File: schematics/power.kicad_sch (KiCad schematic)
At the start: 30 parts, among them J1 9VRMS_60HZ, SW1 SW_SPDT, SW2 SW_Push, SW3 SW_Push, SW4 SW_Push, U1 74HC14, U2 LM2576T-ADJ

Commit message: preliminary PCB design
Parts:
- added H1, H2, H3, H4: MountingHole, MountingHole:MountingHole_3.2mm_M3, symbol Mechanical:MountingHole
- C3, C4, C6, C7: footprint Capacitor_THT:C_Disc_D5.1mm_W3.2mm_P5.00mm -> bvclock:THT_Cap
- D2, D3, D4, D6, D7: footprint Diode_THT:D_DO-35_SOD27_P7.62mm_Horizontal -> bvclock:THT_D_Vertical
- D5: footprint Diode_THT:D_DO-201_P15.24mm_Horizontal -> Diode_THT:D_DO-201AD_P3.81mm_Vertical_CathodeUp
- R1, R2, R3, R4, R5, R6: footprint Resistor_THT:R_Axial_DIN0207_L6.3mm_D2.5mm_P7.62mm_Horizontal -> bvclock:THT_R_Vertical
- U2: footprint Package_TO_SOT_THT:TO-220-5_Vertical -> Package_TO_SOT_THT:TO-220-5_P3.4x3.7mm_StaggerEven_Lead3.8mm_Vertical
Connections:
- net +3V3: now also C5.1, L1.2, R3.1
- net +9VA: now also R1.2; no longer R1.1
- net GND: now also R4.1; no longer R4.2
- net at D2.2 (A), D3.1 (K), U1.1: now also R1.1; no longer R1.2
- net at R3.2, U2.4 (FB): now also R4.2; no longer R4.1
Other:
- moved on the sheet: R1

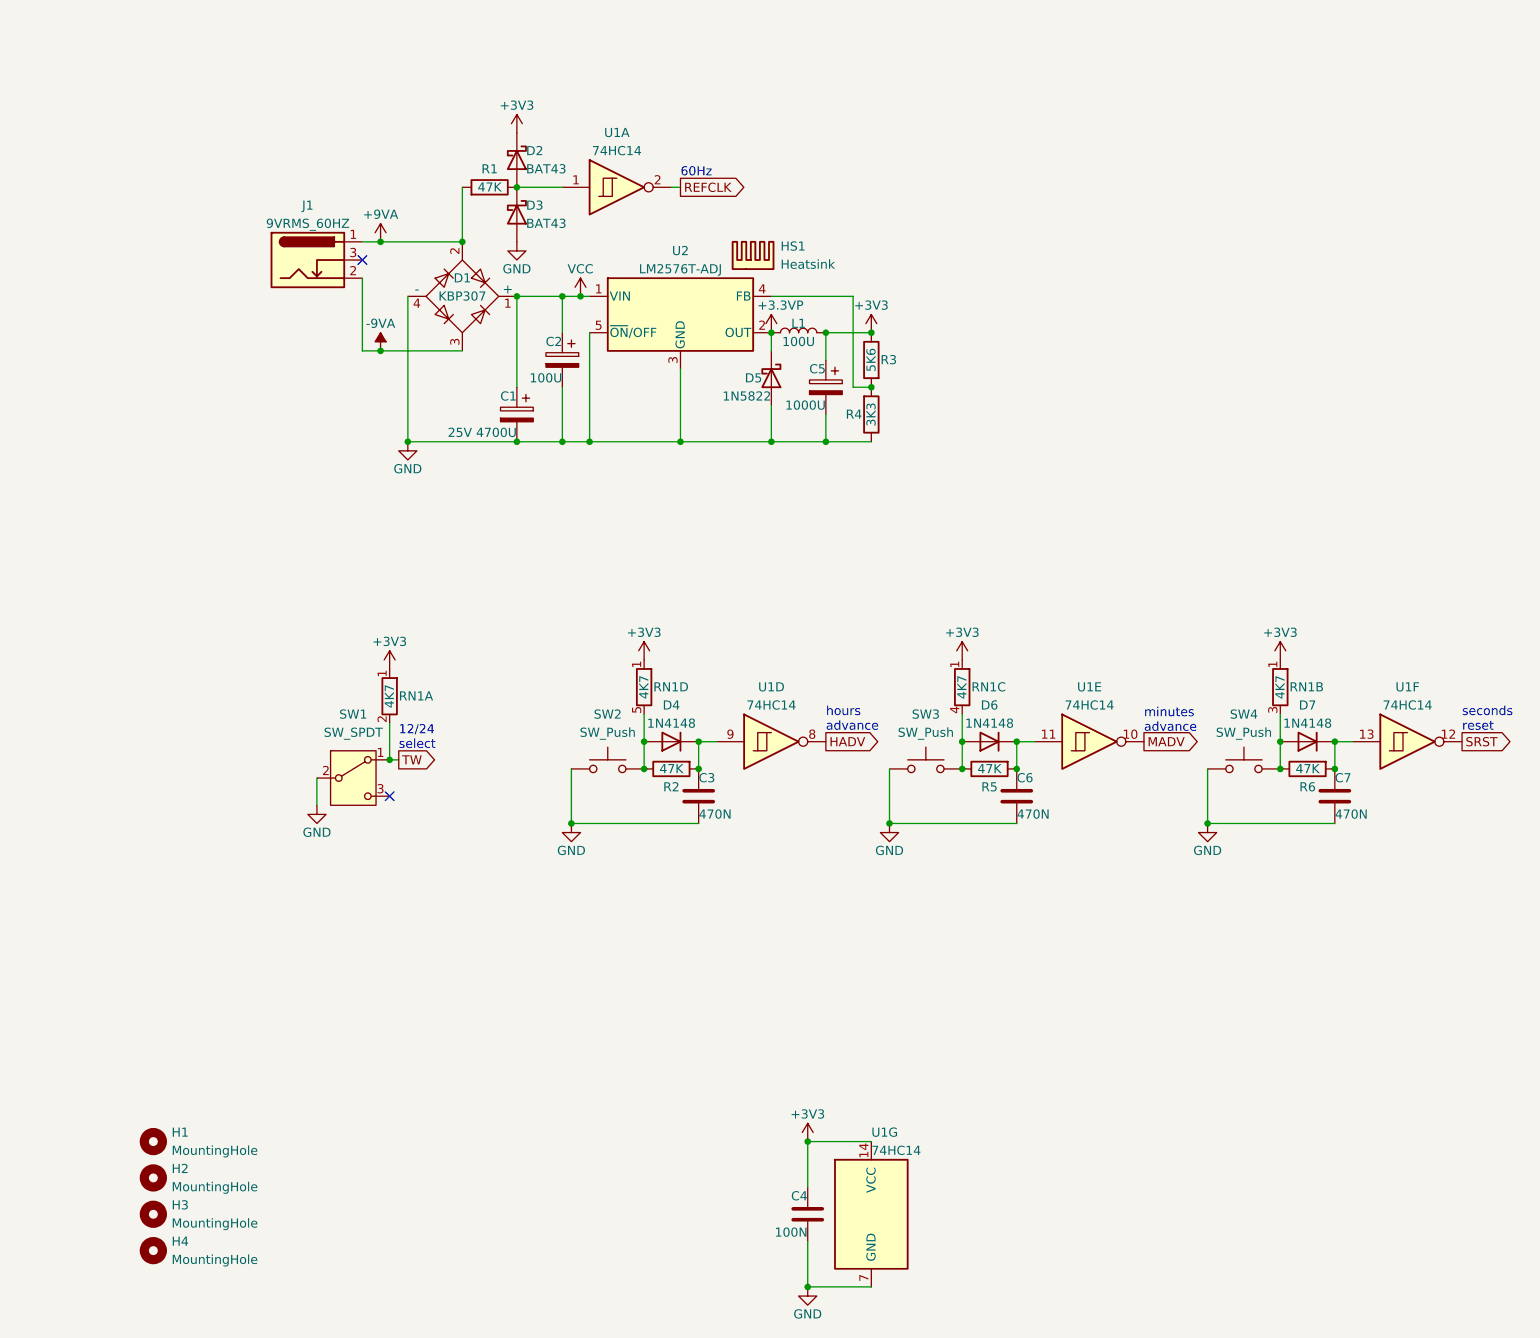
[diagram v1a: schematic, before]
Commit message: passes DRC
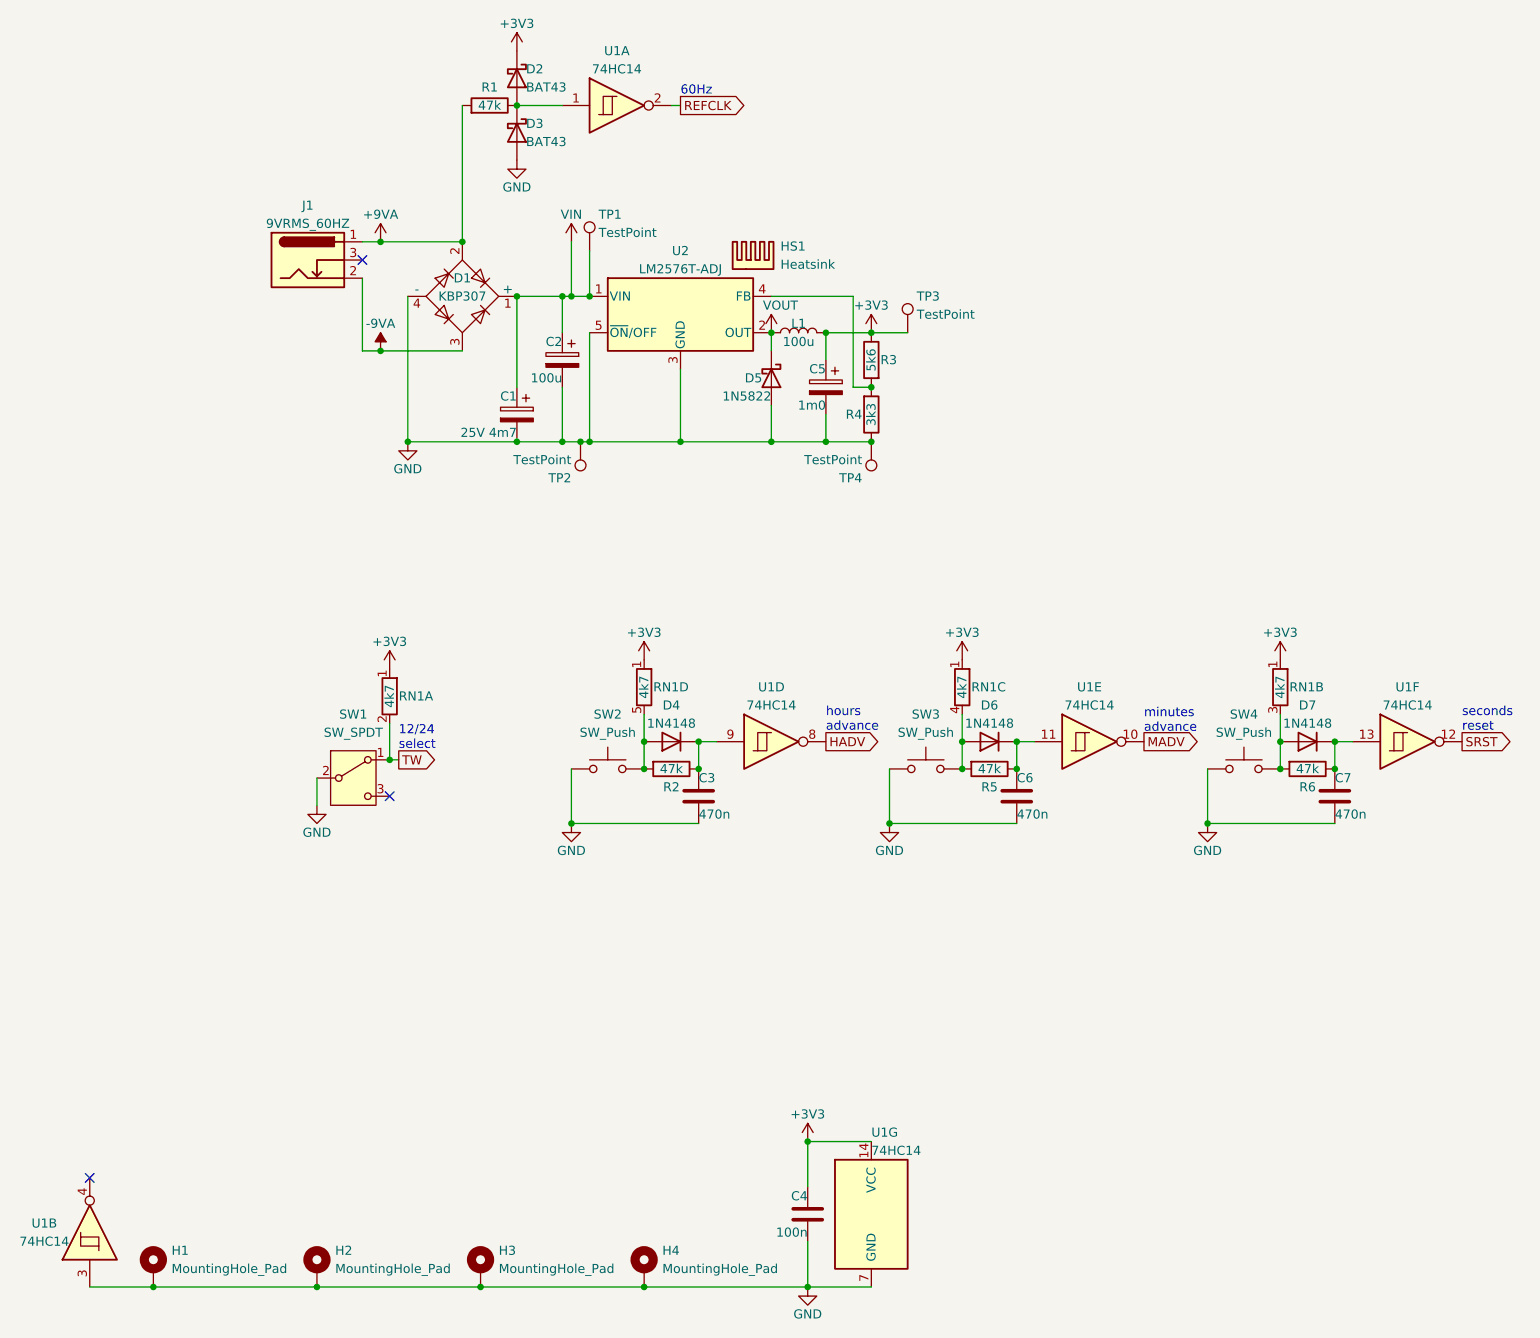
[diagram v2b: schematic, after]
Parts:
- removed H1, H2, H3, H4: MountingHole, MountingHole:MountingHole_3.2mm_M3, symbol Mechanical:MountingHole
- added H1, H2, H3, H4: MountingHole_Pad, MountingHole:MountingHole_2.2mm_M2_ISO7380_Pad_TopBottom, symbol Mechanical:MountingHole_Pad
- added TP1, TP3: TestPoint, bvclock:TestPoint_THTPad_2.5x2.5mm_Drill1.2mm, symbol Connector:TestPoint
- added TP2, TP4: TestPoint, bvclock:TestPoint_THTPad_D1.0mm_Drill0.5mm, symbol Connector:TestPoint
- added unit 2 of U1
- C1: value 25V 4700U -> 25V 4m7
- C2, L1: value 100U -> 100u
- C3, C6, C7: value 470N -> 470n
- C4: value 100N -> 100n
- C5: value 1000U -> 1m0
- D5: footprint Diode_THT:D_DO-201AD_P3.81mm_Vertical_CathodeUp -> Diode_THT:D_DO-201AD_P15.24mm_Horizontal
- J1: footprint Connector_BarrelJack:BarrelJack_Horizontal -> bvclock:BarrelJack_Horizontal
- R1, R2, R5, R6: value 47K -> 47k
- R3: value 5K6 -> 5k6
- R4: value 3K3 -> 3k3
- RN1: value 4K7 -> 4k7
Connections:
- net +3V3: now also TP3.1
- net GND: now also H1.1, H2.1, H3.1, H4.1, TP2.1, TP4.1, U1.3
- net at C3.1, D4.1 (K), U1.9: now also R2.1; no longer R2.2
- net at D6.2 (A), RN1.4 (R3.2), SW3.2: now also R5.2; no longer R5.1
- net at D4.2 (A), RN1.5 (R4.2), SW2.2: now also R2.2; no longer R2.1
- net at D7.2 (A), RN1.3 (R2.2), SW4.2: now also R6.2; no longer R6.1
- net at C6.1, D6.1 (K), U1.11: now also R5.1; no longer R5.2
- net at C7.1, D7.1 (K), U1.13: now also R6.1; no longer R6.2
- net +3.3VP renamed VOUT
- net VCC renamed VIN
- net VIN: now also TP1.1
- no-connect marks 2 -> 3
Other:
- moved on the sheet: D2, D3, R1, R2, R5, R6, U1A

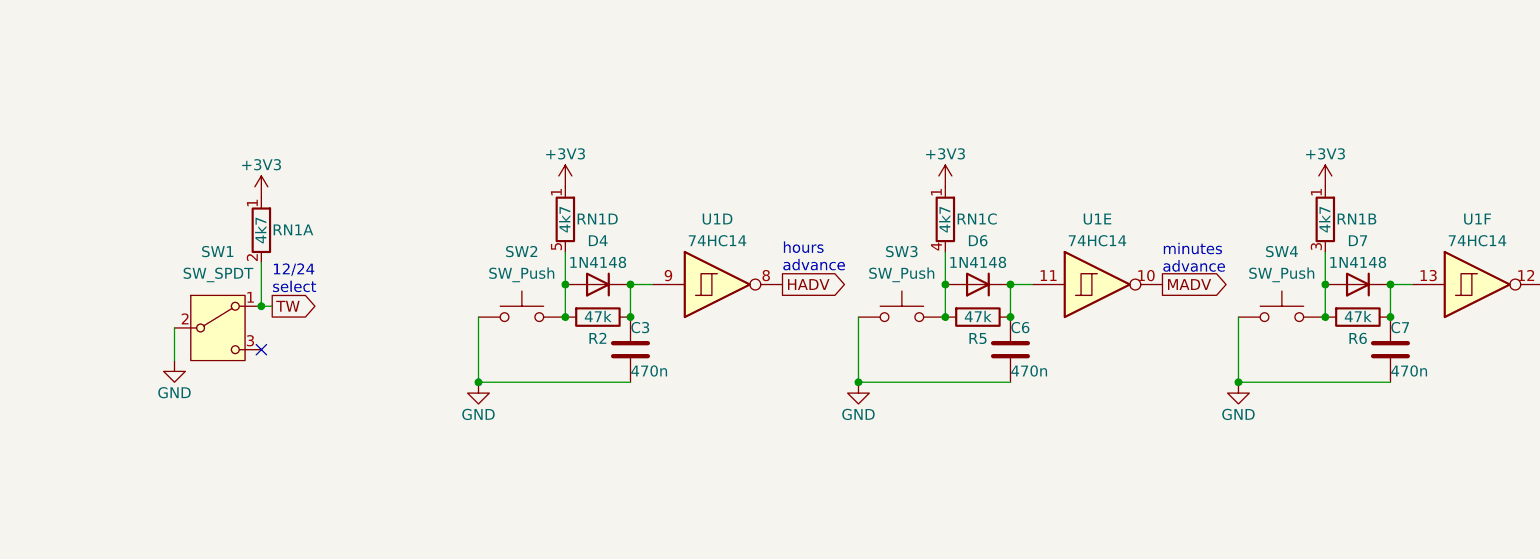
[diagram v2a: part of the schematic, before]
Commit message: switch fix, testpoint for DEMOUT, rearrange resistors
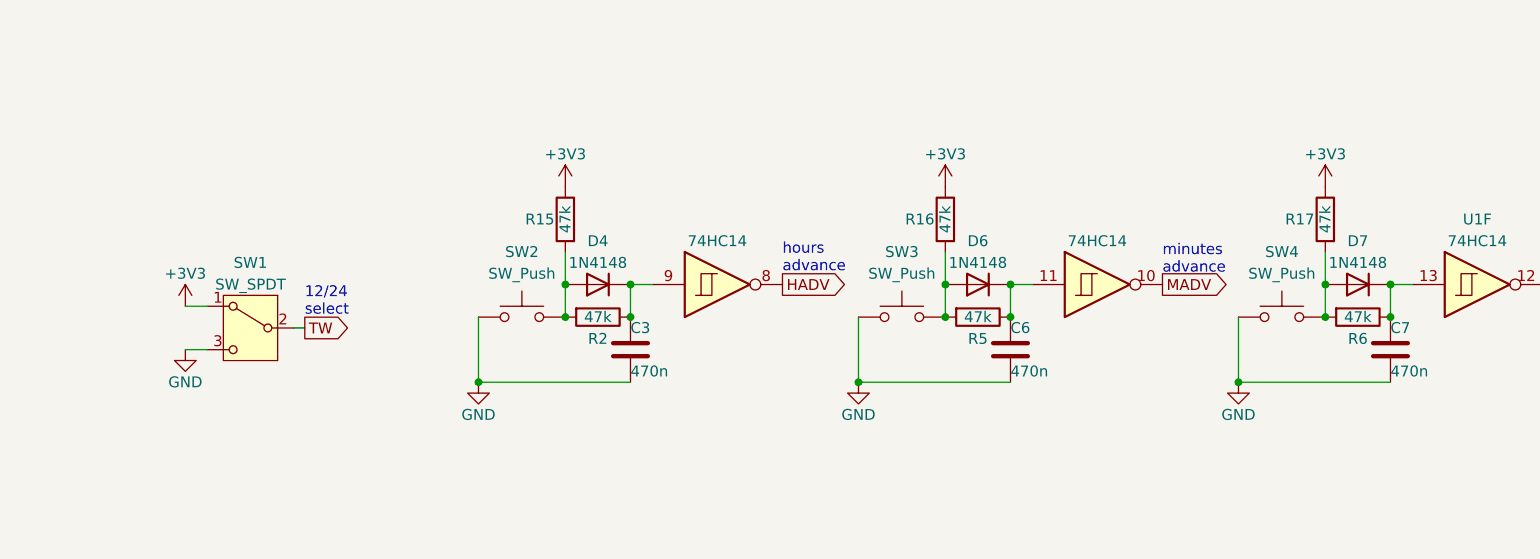
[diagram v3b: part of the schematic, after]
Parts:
- removed RN1: 4k7, Resistor_THT:R_Array_SIP5, symbol Device:R_Network04_Split
- added R15, R16, R17: 47k, bvclock:THT_R_Vertical, symbol Device:R
- U2: footprint Package_TO_SOT_THT:TO-220-5_P3.4x3.7mm_StaggerEven_Lead3.8mm_Vertical -> bvclock:TO-220-5_Vertical_HandSolder
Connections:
- net +3V3: now also SW1.1 (A), R15.1, R16.1, R17.1
- net GND: now also SW1.3 (C); no longer SW1.2 (B)
- net TW: now also SW1.2 (B); no longer SW1.1 (A)
- net at D6.2 (A), R5.2, SW3.2: now also R16.2
- net at D4.2 (A), R2.2, SW2.2: now also R15.2
- net at D7.2 (A), R6.2, SW4.2: now also R17.2
- no-connect marks 3 -> 2
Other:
- moved on the sheet: SW1

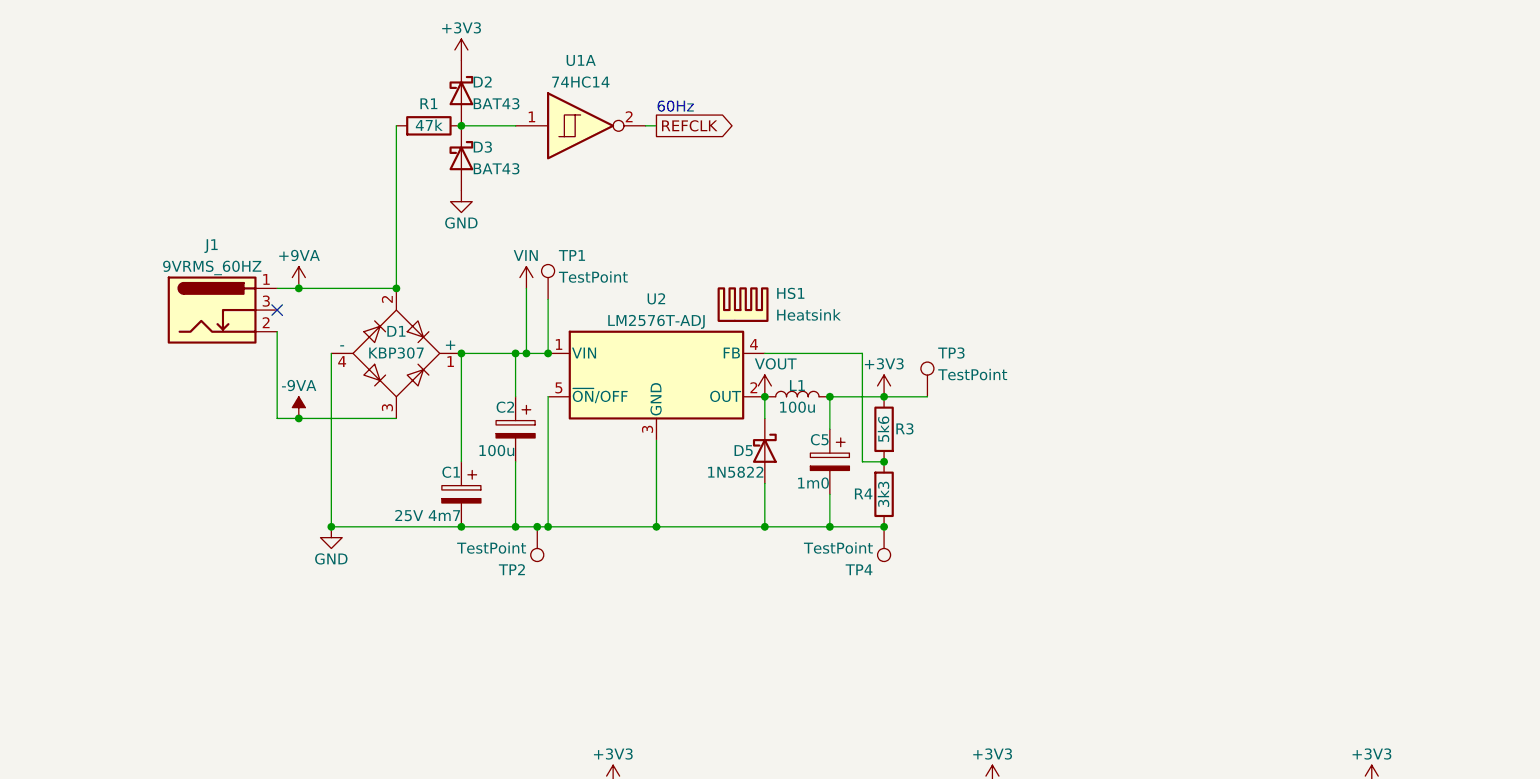
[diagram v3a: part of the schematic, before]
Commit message: changed buck converter
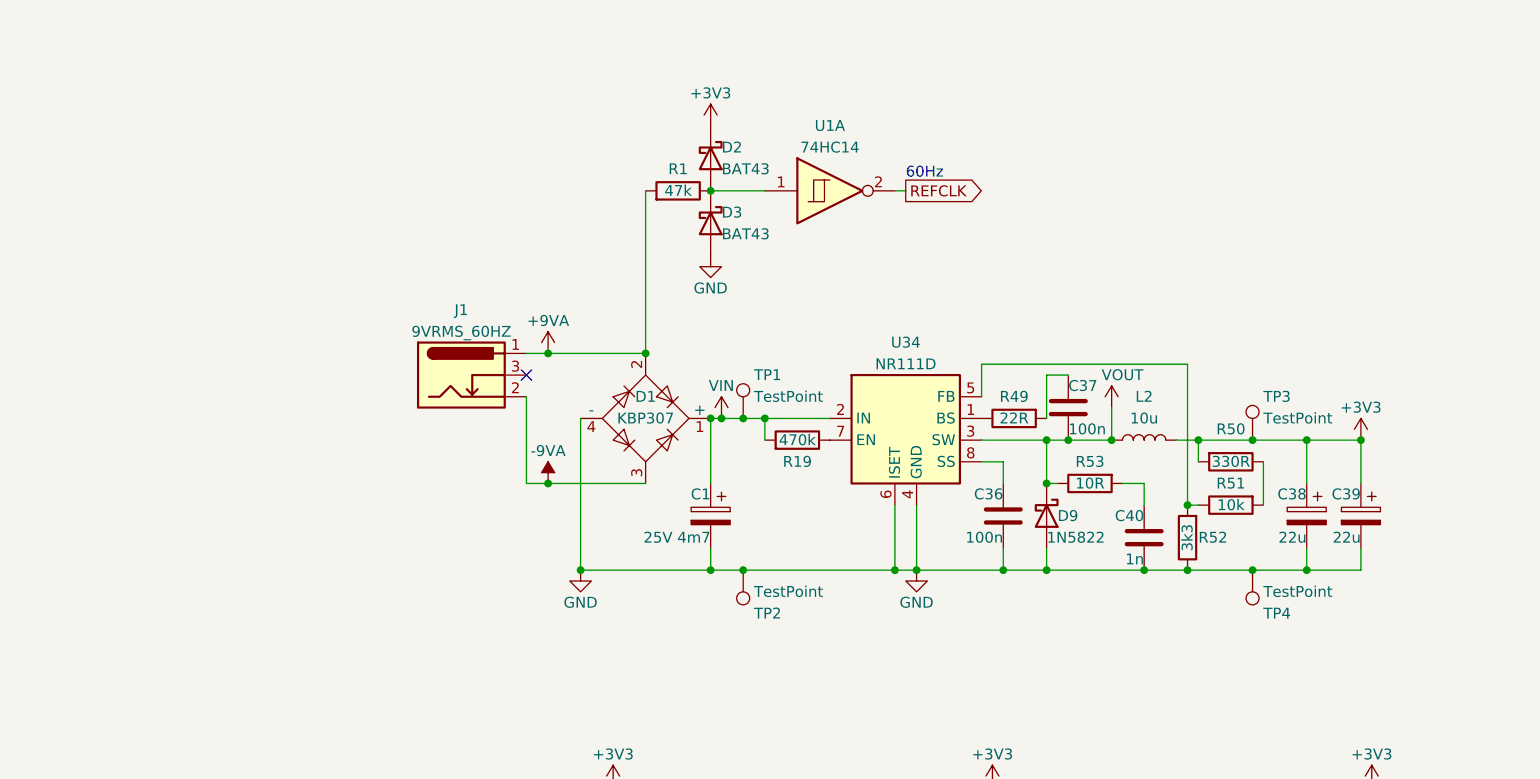
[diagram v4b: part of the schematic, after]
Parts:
- removed C2: 100u, Capacitor_THT:CP_Radial_D5.0mm_P2.00mm, symbol Device:C_Polarized
- removed C5: 1m0, Capacitor_THT:CP_Radial_D10.0mm_P5.00mm, symbol Device:C_Polarized
- removed D5: 1N5822, Diode_THT:D_DO-201AD_P15.24mm_Horizontal, symbol Device:D_Schottky
- removed HS1: Heatsink, bvclock:Heatsink_TO-220, symbol Mechanical:Heatsink
- removed L1: 100u, Inductor_THT:L_Toroid_Vertical_L14.7mm_W8.6mm_P5.58mm_Pulse_KM-1, symbol Device:L
- removed R3: 5k6, bvclock:THT_R_Vertical, symbol Device:R
- removed R4: 3k3, bvclock:THT_R_Vertical, symbol Device:R
- removed U2: LM2576T-ADJ, bvclock:TO-220-5_Vertical_HandSolder, symbol Regulator_Switching:LM2576T-ADJ
- added C36, C37: 100n, bvclock:THT_Cap, symbol Device:C
- added C38, C39: 22u, Capacitor_THT:CP_Radial_D5.0mm_P2.00mm, symbol Device:C_Polarized
- added C40: 1n, bvclock:THT_Cap, symbol Device:C
- added D9: 1N5822, Diode_THT:D_DO-201AD_P15.24mm_Horizontal, symbol Device:D_Schottky
- added L2: 10u, Inductor_THT:L_Radial_D7.0mm_P3.00mm, symbol Device:L
- added R19: 470k, bvclock:THT_R_Vertical, symbol Device:R
- added R49: 22R, bvclock:THT_R_Vertical, symbol Device:R
- added R50: 330R, bvclock:THT_R_Vertical, symbol Device:R
- added R51: 10k, bvclock:THT_R_Vertical, symbol Device:R
- added R52: 3k3, bvclock:THT_R_Vertical, symbol Device:R
- added R53: 10R, bvclock:THT_R_Vertical, symbol Device:R
- added U34: NR111D, Package_DIP:DIP-8_W7.62mm, symbol bvclock:NR111D
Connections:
- net +3V3: now also C38.1, C39.1, L2.2, R50.2
- net GND: now also C36.2, C38.2, C39.2, C40.2, D9.2 (A), R52.1, U34.4 (GND), U34.6 (ISET)
- net VIN: now also R19.2, U34.2 (IN)
- net VOUT: now also C37.2, D9.1 (K), L2.1, R53.1, U34.3 (SW)
- new net: R50.1, R51.2
- new net: C36.1, U34.8 (SS)
- new net: R19.1, U34.7 (EN)
- new net: R49.1, U34.1 (BS)
- new net: C37.1, R49.2
- new net: R51.1, R52.2, U34.5 (FB)
- new net: C40.1, R53.2
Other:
- moved on the sheet: C1, D1, D2, D3, J1, R1, U1A
